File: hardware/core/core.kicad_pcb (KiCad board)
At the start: 4 copper layers, 31.3 x 67.7 mm, 43 parts, among them J17 PROG, J5 TO_NEXT, J7 TO_NEXT, J8 Conn_02x09_Odd_Even, SW1 RESET, SW2 BOOT, U10 SN74AHCT1G14DCKR, U19 ESP32-S3-MINI-1, U20 AP2112K-3.3TRG1, U21 SN65HVD230DR

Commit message: feat(hardware): update core USB-C connector
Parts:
- removed USBC1: TYPE-C-31-M-12, SpaghettiLAB:USB-C_SMD-TYPE-C-31-M-12_1
- added U1: HC-TYPE-C-16P-01A, SpaghettiLAB:USB-C-SMD_HC-TYPE-C-16P-01A, F.Cu at (71.4, 128.7)
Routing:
- net Net-(U1-CC1): track 0.00 -> 2.51 mm, vias 0 -> 1
- net Net-(USBC1-CC1): track 2.04 -> 0.00 mm, vias 1 -> 0
- net VBUS: track 7.00 -> 7.61 mm
- net Net-(R18-Pad2): track 10.0 -> 10.6 mm

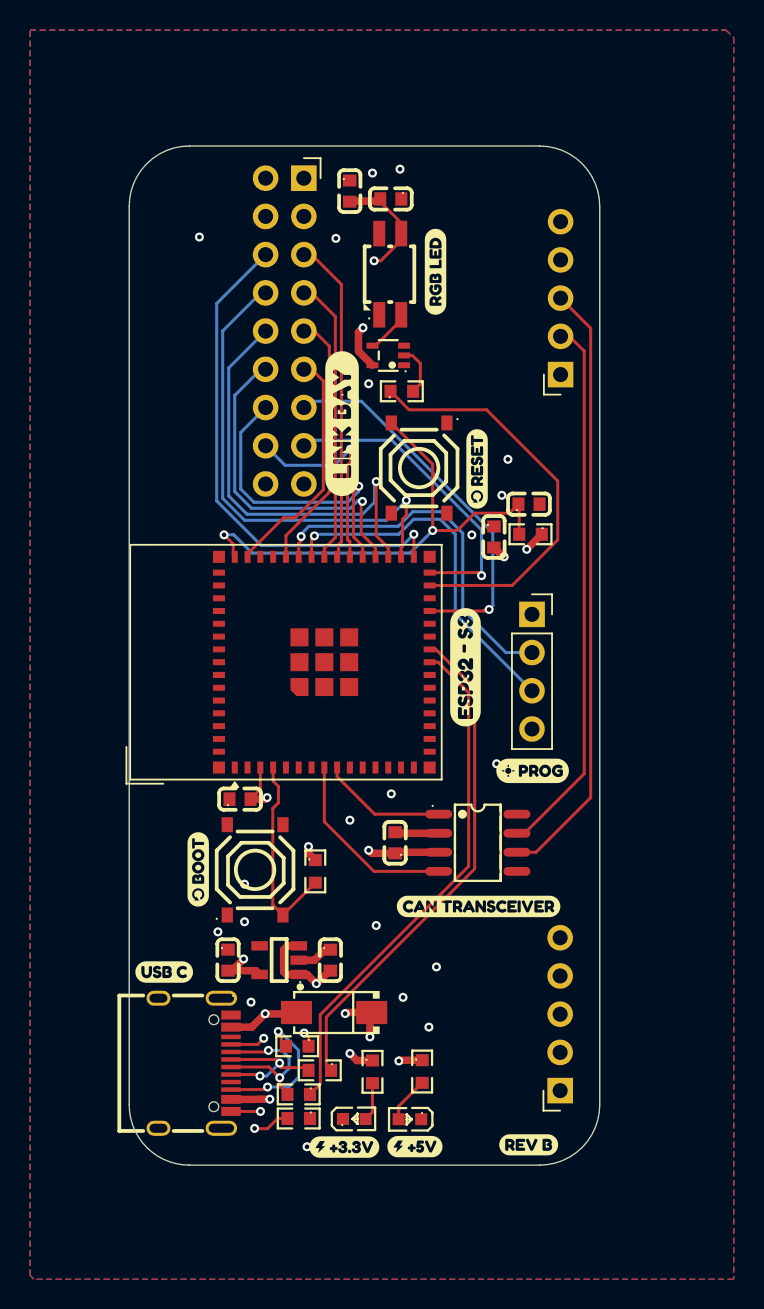
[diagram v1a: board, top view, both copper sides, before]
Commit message: Fixed silkscreen text
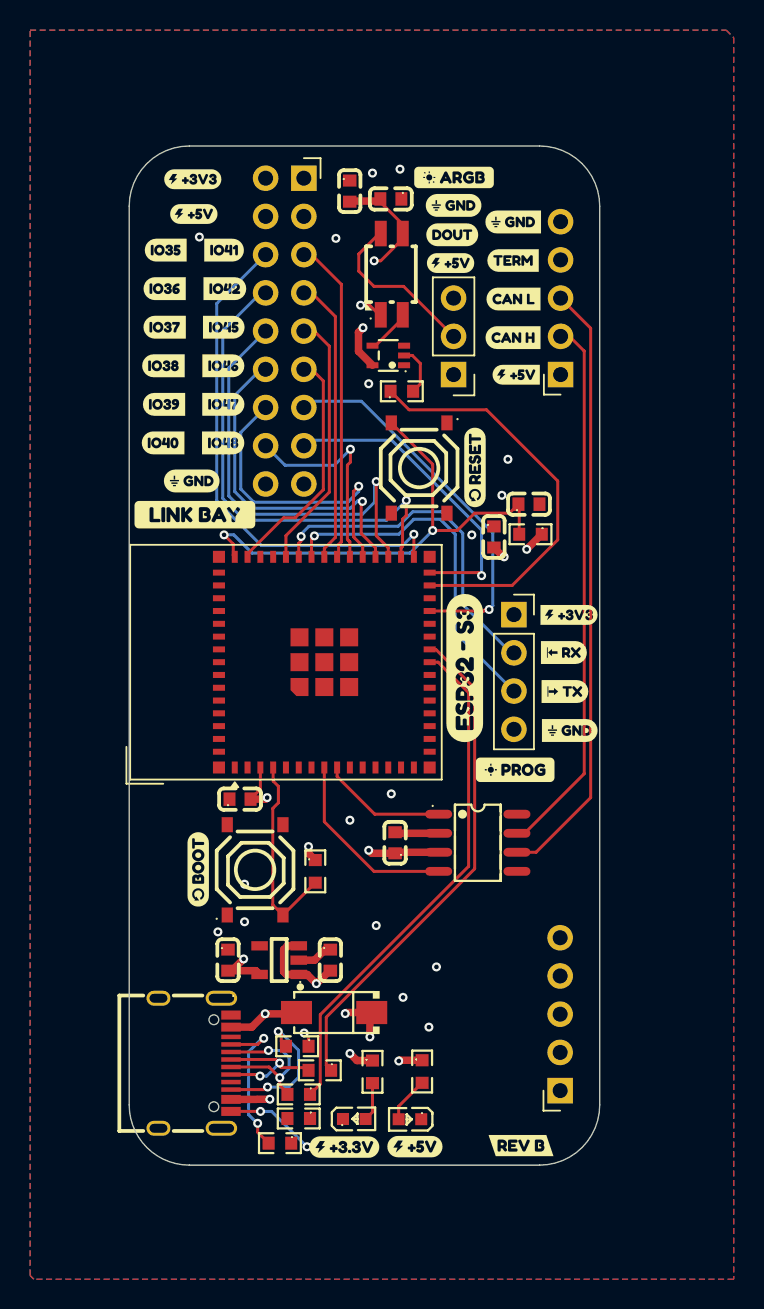
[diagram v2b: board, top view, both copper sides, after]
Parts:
- removed kobee-studio-6AA83E1F, kobee-studio-6AA83E5B, kobee-studio-6AA83EFB: Kobee Studio, kobee-studio-6AA83D3C
- added J1: ARGB, Connector_PinHeader_2.54mm:PinHeader_1x03_P2.54mm_Vertical, F.Cu at (88.6, 82.9)
- added R23: 5.1k, SpaghettiLAB:R0603, F.Cu at (77.1, 134.0)
- added kobee-studio-6AA91493: Kobee Studio, kobee-studio-6AA83D3C, F.Cu at (71.2, 90.0)
- added kobee-studio-6AA91493: Kobee Studio, kobee-studio-6AA83D3C, F.Cu at (88.6, 71.7)
- added kobee-studio-6AA914C2: Kobee Studio, kobee-studio-6AA83D3C, F.Cu at (71.3, 69.9)
- added kobee-studio-6AA915EE: Kobee Studio, kobee-studio-6AA83D3C, F.Cu at (71.4, 72.2)
- added kobee-studio-6AA915EE: Kobee Studio, kobee-studio-6AA83D3C, F.Cu at (88.4, 75.5)
- added kobee-studio-6AA91E4F: Kobee Studio, kobee-studio-6AA83D3C, F.Cu at (88.5, 73.6)
- added kobee-studio-6AA91FA3: Kobee Studio, kobee-studio-6AA83D3C, F.Cu at (92.8, 82.9)
- added kobee-studio-6AA91FB4: Kobee Studio, kobee-studio-6AA83D3C, F.Cu at (92.6, 80.4)
- added kobee-studio-6AA91FC0: Kobee Studio, kobee-studio-6AA83D3C, F.Cu at (92.6, 77.9)
- added kobee-studio-6AA91FC9: Kobee Studio, kobee-studio-6AA83D3C, F.Cu at (92.6, 75.3)
- added kobee-studio-6AA91FD2: Kobee Studio, kobee-studio-6AA83D3C, F.Cu at (92.6, 72.8)
- added kobee-studio-6AA92015: Kobee Studio, kobee-studio-6AA83D3C, F.Cu at (96.3, 98.9)
- added kobee-studio-6AA9201C: Kobee Studio, kobee-studio-6AA83D3C, F.Cu at (96.0, 101.4)
- added kobee-studio-6AA92023: Kobee Studio, kobee-studio-6AA83D3C, F.Cu at (96.0, 104.0)
- added kobee-studio-6AA92029: Kobee Studio, kobee-studio-6AA83D3C, F.Cu at (96.4, 106.5)
- added kobee-studio-6AA9246B: Kobee Studio, kobee-studio-6AA83D3C, F.Cu at (69.5, 74.6)
- added kobee-studio-6AA92476: Kobee Studio, kobee-studio-6AA83D3C, F.Cu at (69.4, 77.2)
- added kobee-studio-6AA9247D: Kobee Studio, kobee-studio-6AA83D3C, F.Cu at (69.4, 79.7)
- added kobee-studio-6AA92486: Kobee Studio, kobee-studio-6AA83D3C, F.Cu at (69.4, 82.3)
- added kobee-studio-6AA9248F: Kobee Studio, kobee-studio-6AA83D3C, F.Cu at (69.4, 84.9)
- added kobee-studio-6AA924CD: Kobee Studio, kobee-studio-6AA83D3C, F.Cu at (69.3, 87.4)
- added kobee-studio-6AA9311E: Kobee Studio, kobee-studio-6AA83D3C, F.Cu at (73.3, 87.4)
- added kobee-studio-6AA93134: Kobee Studio, kobee-studio-6AA83D3C, F.Cu at (73.3, 84.9)
- added kobee-studio-6AA9313B: Kobee Studio, kobee-studio-6AA83D3C, F.Cu at (73.3, 82.3)
- added kobee-studio-6AA93141: Kobee Studio, kobee-studio-6AA83D3C, F.Cu at (73.4, 79.7)
- added kobee-studio-6AA93147: Kobee Studio, kobee-studio-6AA83D3C, F.Cu at (73.4, 77.2)
- added kobee-studio-6AA9314C: Kobee Studio, kobee-studio-6AA83D3C, F.Cu at (73.4, 74.6)
- added kobee-studio-6AA93394: Kobee Studio, kobee-studio-6AA91E6F, F.Cu at (88.7, 69.8)
- C14, C24, C73, C74, C75, C76, C77, C78: footprint SpaghettiLAB2:C0603 -> SpaghettiLAB:C0603
- D2, D3: footprint SpaghettiLAB2:LED0603-RD -> SpaghettiLAB:LED0603-RD
- LED2: footprint SpaghettiLAB2:LED-SMD_4P-L3.2-W2.8-LS5.9_SK6812MINI-E -> SpaghettiLAB:LED-SMD_4P-L3.2-W2.8-LS5.9_SK6812MINI-E
- R10, R15, R16, R17, R18, R20, R21, R22: footprint SpaghettiLAB2:R0603 -> SpaghettiLAB:R0603
- SW1, SW2: footprint SpaghettiLAB2:SW-SMD_4P-L5.1-W5.1-P3.70-LS6.5-TL_H1.5 -> SpaghettiLAB:SW-SMD_4P-L5.1-W5.1-P3.70-LS6.5-TL_H1.5
- U10: footprint SpaghettiLAB2:SOT-353_L2.2-W1.4-P0.65-LS2.4-BR -> SpaghettiLAB:SOT-353_L2.2-W1.4-P0.65-LS2.4-BR
- U20: footprint SpaghettiLAB2:SOT-25-5_L2.9-W1.6-P0.95-LS2.8-BL -> SpaghettiLAB:SOT-25-5_L2.9-W1.6-P0.95-LS2.8-BL
- moved kobee-studio-6AA93383 11.5 mm to (71.5, 92.2), turned to 0 degrees
- moved J17 1.20 mm to (92.7, 98.8)
- moved kobee-studio-6AA9337A 1.16 mm to (92.7, 109.2)
- moved kobee-studio-6AA92049 0.51 mm to (93.1, 134.1)
- moved kobee-studio-6AA93221 0.17 mm to (90.1, 89.1)
- moved kobee-studio-6AA91364 0.07 mm to (89.4, 102.4)
- renumbered kobee-studio-6AA83FED to kobee-studio-6AA91364, kobee-studio-6AA83E8C to kobee-studio-6AA92049, kobee-studio-6AA83E19 to kobee-studio-6AA93221, kobee-studio-6AA83FBE to kobee-studio-6AA9337A, kobee-studio-6AA83D3C to kobee-studio-6AA93383
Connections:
- net Net-(J17-Pin_2) renamed /PROG_RX
- net Net-(J17-Pin_3) renamed /PROG_TX
- net Net-(U1-CC2) renamed /CC2
- LED2 pad 4: unconnected-(LED2-DOUT-Pad4) -> /DOUT
- U1 pad A5: Net-(U1-CC1) -> /CC1
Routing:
- net /DOUT: track 0.00 -> 11.2 mm
- net /CC1: track 0.00 -> 10.6 mm, vias 0 -> 2
- net GND: track 9.81 -> 15.4 mm, vias 21 -> 22
- net Net-(U1-CC1): track 2.51 -> 0.00 mm, vias 1 -> 0
- net Net-(J18-CC2): track 2.47 -> 0.00 mm, vias 1 -> 0
- net /PROG_RX: track 24.4 -> 23.4 mm
- net VCORE: vias 8 -> 7

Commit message: minor changes
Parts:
- moved J5 0.80 mm to (96.5, 82.9)
- moved J7 0.76 mm to (96.5, 130.4)
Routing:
- net CORE_CANL: track 40.4 -> 41.9 mm

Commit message: Changed link bay connector disposition
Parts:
- added kobee-studio-6AABEB02: Kobee Studio, kobee-studio-6AA83D3C, F.Cu at (79.7, 91.6)
- added kobee-studio-6AABEB18: Kobee Studio, kobee-studio-6AA83D3C, F.Cu at (79.4, 73.8)
- added kobee-studio-6AABEB1D: Kobee Studio, kobee-studio-6AA83D3C, F.Cu at (79.7, 71.2)
- moved kobee-studio-6AABEAAD 23.5 mm to (75.2, 69.0)
- moved kobee-studio-6AA9313B 6.22 mm to (79.3, 84.2)
- moved kobee-studio-6AA93141 6.18 mm to (79.3, 81.6)
- moved kobee-studio-6AA9311E 6.17 mm to (79.2, 89.3)
- moved kobee-studio-6AA93134 6.16 mm to (79.2, 86.7)
- moved kobee-studio-6AA93147 6.16 mm to (79.3, 79.0)
- moved kobee-studio-6AA9314C 6.11 mm to (79.2, 76.5)
- moved C14 2.96 mm to (84.4, 69.5), turned to 180 degrees
- moved kobee-studio-6AA92476 2.43 mm to (71.1, 78.9)
- moved kobee-studio-6AA9246B 2.43 mm to (71.2, 76.4)
- moved kobee-studio-6AA92486 2.42 mm to (71.1, 84.0)
- moved kobee-studio-6AA9248F 2.29 mm to (71.1, 86.4)
- moved kobee-studio-6AA9247D 2.28 mm to (71.1, 81.3)
- moved kobee-studio-6AA924CD 2.27 mm to (71.0, 88.9)
- moved J8 2.16 mm to (76.5, 69.7)
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- renumbered kobee-studio-6AA93383 to kobee-studio-6AABEAAD, kobee-studio-6AA91493 to kobee-studio-6AABEB0E, kobee-studio-6AA915EE to kobee-studio-6AABEB2F, kobee-studio-6AA914C2 to kobee-studio-6AABEB3C
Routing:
- net 5V: track 23.0 -> 83.1 mm
- net GND: track 15.4 -> 39.3 mm, vias 22 -> 20
- net VCORE: track 17.1 -> 31.8 mm
- net IO36: track 32.3 -> 23.7 mm
- net IO37: track 29.4 -> 21.6 mm
- net IO35: track 34.0 -> 26.5 mm
- net IO39: track 20.2 -> 22.9 mm
- net IO38: track 22.5 -> 25.1 mm
- net IO40: track 13.8 -> 16.3 mm
- net IO48: track 21.0 -> 23.0 mm
- net IO47: track 25.5 -> 27.4 mm
- net IO46: track 15.8 -> 15.2 mm
- net IO41: track 21.5 -> 22.0 mm

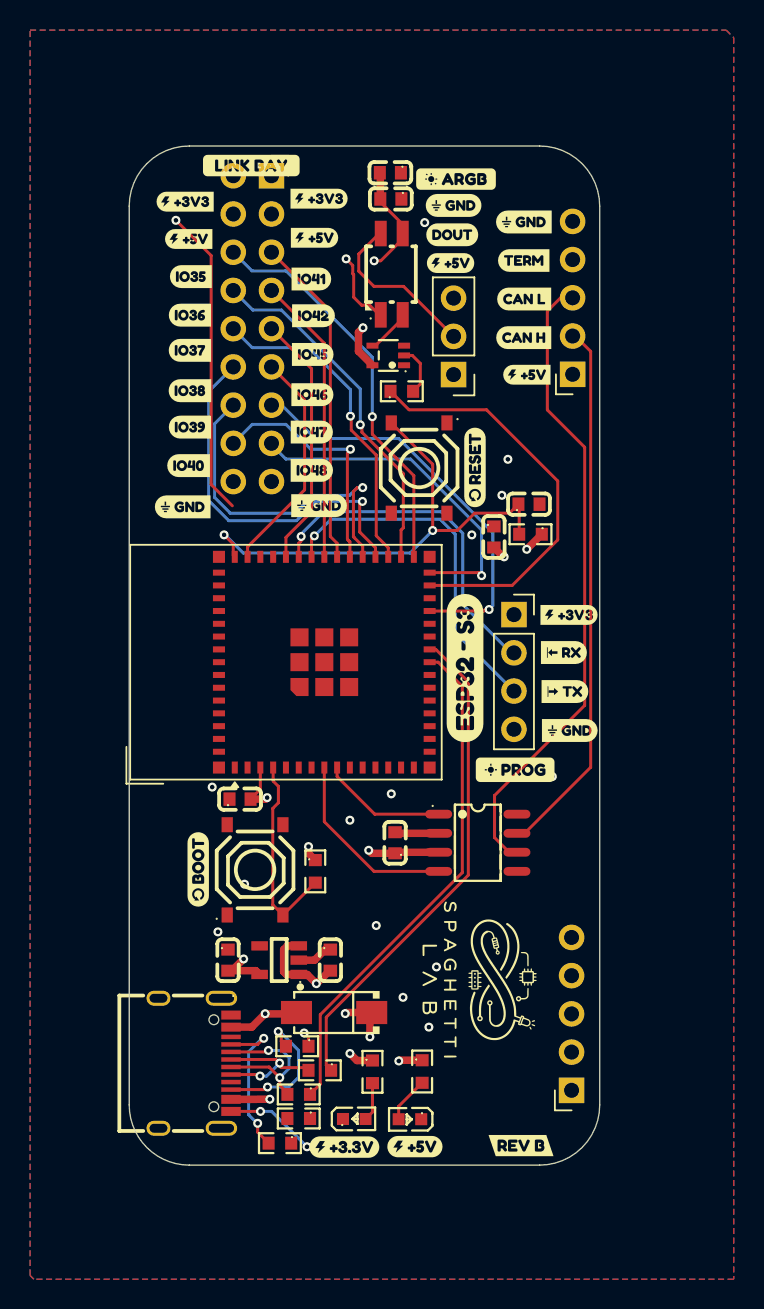
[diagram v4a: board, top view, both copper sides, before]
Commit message: removed rgb led from core
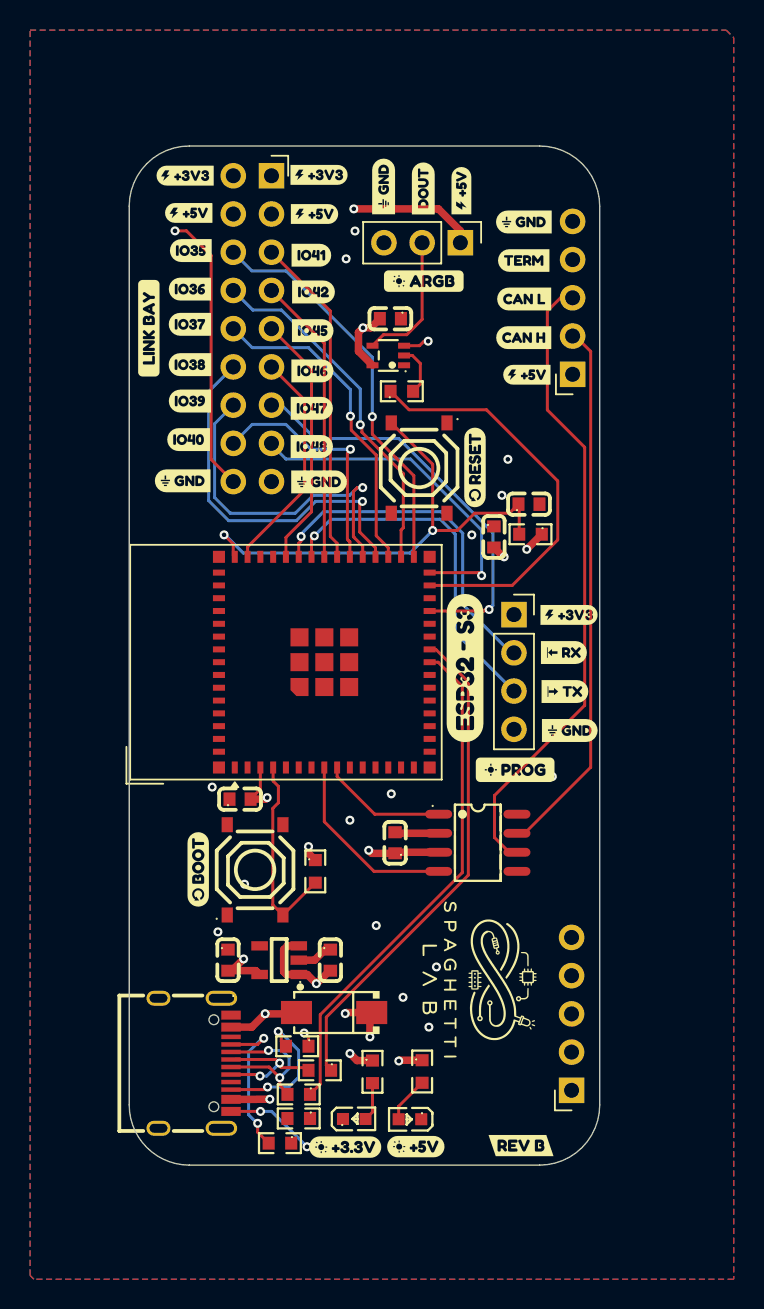
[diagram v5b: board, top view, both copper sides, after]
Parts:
- removed C24: 100nF, SpaghettiLAB:C0603
- removed LED2: SK6812MINI-E, SpaghettiLAB:LED-SMD_4P-L3.2-W2.8-LS5.9_SK6812MINI-E
- moved kobee-studio-6AABEAAD 12.8 mm to (68.4, 79.8), turned to 90 degrees
- moved C14 9.70 mm to (84.4, 79.2)
- moved J1 8.77 mm to (89.1, 74.1), turned to -90 degrees
- moved kobee-studio-6AA93394 7.11 mm to (86.7, 76.7)
- moved kobee-studio-6AACD940 4.86 mm to (89.2, 70.7), turned to 90 degrees
- moved kobee-studio-6AACD935 4.82 mm to (84.0, 70.4), turned to 90 degrees
- moved kobee-studio-6AACD93B 3.63 mm to (86.6, 70.5), turned to 90 degrees
- moved kobee-studio-6AA92476 1.73 mm to (71.1, 77.2)
- moved kobee-studio-6AA9247D 1.73 mm to (71.1, 79.5)
- moved kobee-studio-6AA924CD 1.73 mm to (71.0, 87.2)
- moved kobee-studio-6AABEB0E 1.73 mm to (70.6, 90.0)
- moved kobee-studio-6AABEB3C 1.73 mm to (70.8, 69.7)
- moved kobee-studio-6AA9246B 1.73 mm to (71.2, 74.7)
- moved kobee-studio-6AA92486 1.73 mm to (71.1, 82.2)
- moved kobee-studio-6AA9248F 1.73 mm to (71.1, 84.7)
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- renumbered kobee-studio-6AA91493 to kobee-studio-6AACD935, kobee-studio-6AA91E4F to kobee-studio-6AACD93B, kobee-studio-6AA915EE to kobee-studio-6AACD940, kobee-studio-6AA83ED5 to kobee-studio-6AACD9C8, kobee-studio-6AA83EC3 to kobee-studio-6AACD9D1
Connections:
- U10 pad 4: Net-(LED2-DIN) -> /DOUT
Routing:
- net GND: track 39.3 -> 34.3 mm, vias 20 -> 21
- net Net-(LED2-DIN): track 2.96 -> 0.00 mm
- net 5V: track 83.1 -> 85.3 mm
- net /DOUT: track 11.2 -> 9.11 mm
